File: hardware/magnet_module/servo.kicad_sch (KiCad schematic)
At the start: 5 parts, among them J21 Conn_01x03_Pin, J4 Conn_01x03_Pin, U6 TXB0102DCU

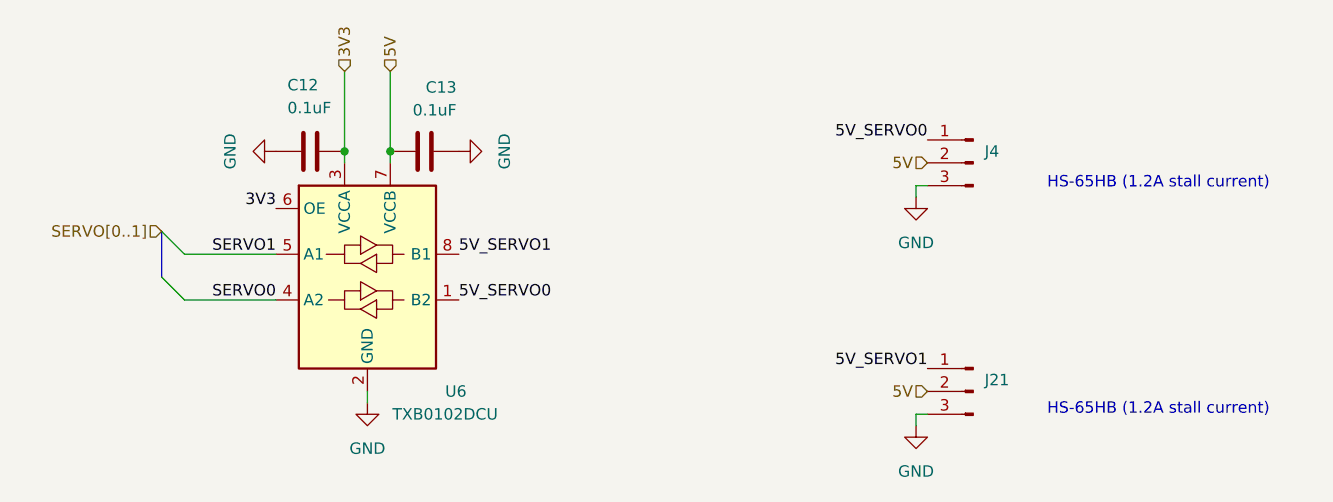
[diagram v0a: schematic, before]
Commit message: Make schematic changes for the following v1.1 changes: * Add directional & latching connector to GPIO0 & GPIO1 * Add CAN IN / CAN OUT directionality * Add pulldown to BOOT pin and pullup to nRST * Correct servo orientation
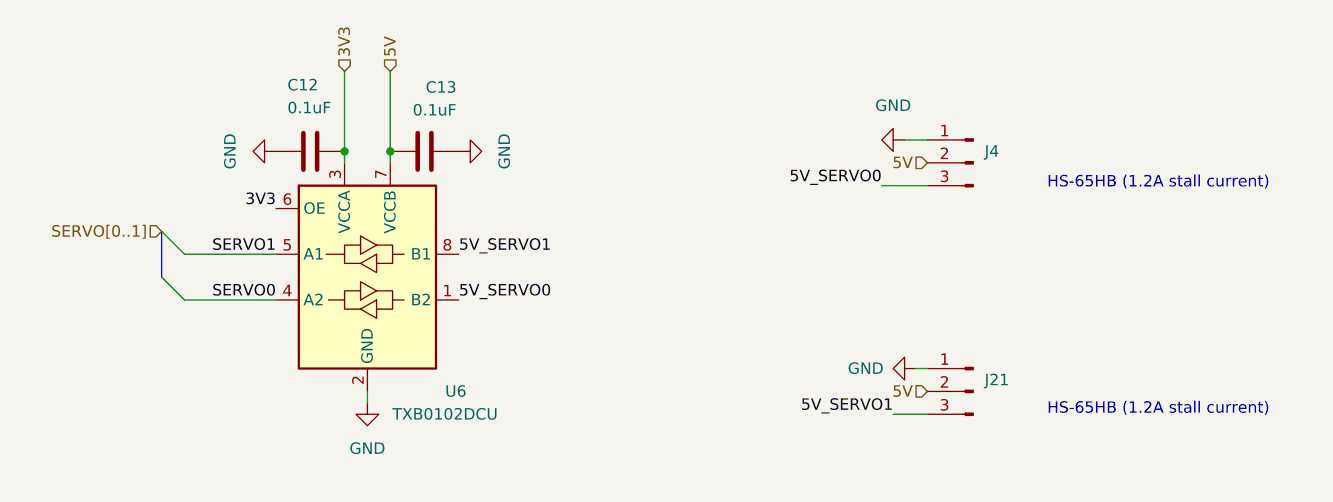
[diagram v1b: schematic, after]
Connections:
- net 5V_SERVO0: now also J4.3 (Pin_3); no longer J4.1 (Pin_1)
- net 5V_SERVO1: now also J21.3 (Pin_3); no longer J21.1 (Pin_1)
- net GND: now also J21.1 (Pin_1), J4.1 (Pin_1); no longer J21.3 (Pin_3), J4.3 (Pin_3)
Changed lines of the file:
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@@
+	(wire
+		(pts
+			(xy 125.73 96.52) (xy 128.27 96.52)
+		)
+		(stroke
+			(width 0)
+			(type default)
+		)
+	)
 	(wire
 		(pts
@@
 	(wire
 		(pts
-			(xy 127 101.6) (xy 127 102.87)
+			(xy 128.27 121.92) (xy 127 121.92)
 		)
 		(stroke
@@
 	(wire
 		(pts
-			(xy 128.27 127) (xy 127 127)
+			(xy 45.72 109.22) (xy 55.88 109.22)
 		)
 		(stroke
@@
 	(wire
 		(pts
-			(xy 45.72 109.22) (xy 55.88 109.22)
+			(xy 124.46 127) (xy 128.27 127)
 		)
 		(stroke
@@
 	(wire
 		(pts
-			(xy 128.27 101.6) (xy 127 101.6)
+			(xy 128.27 101.6) (xy 123.19 101.6)
 		)
 		(stroke
@@
 		)
 	)
-	(wire
-		(pts
-			(xy 127 127) (xy 127 128.27)
-		)
-		(stroke
-			(width 0)
-			(type default)
-		)
-	)
 	(text "HS-65HB (1.2A stall current)"
 		(exclude_from_sim no)
@@
 	)
 	(label "5V_SERVO1"
-		(at 128.27 121.92 180)
+		(at 124.46 127 180)
 		(fields_autoplaced yes)
 		(effects
@@
 	)
 	(label "5V_SERVO0"
-		(at 128.27 96.52 180)
+		(at 123.19 101.6 180)
 		(fields_autoplaced yes)
 		(effects
@@
 	(symbol
 		(lib_id "power:GND")
-		(at 127 102.87 0)
+		(at 125.73 96.52 270)
 		(unit 1)
 		(exclude_from_sim no)
@@
 		(fields_autoplaced yes)
 		(property "Reference" "#PWR011"
-			(at 127 109.22 0)
+			(at 119.38 96.52 0)
 			(effects
 				(font
@@
 		)
 		(property "Value" "GND"
-			(at 127 107.95 0)
+			(at 124.46 92.71 90)
 			(effects
 				(font
@@
 		)
 		(property "Footprint" ""
-			(at 127 102.87 0)
+			(at 125.73 96.52 0)
 			(effects
 				(font
@@
 		)
 		(property "Datasheet" ""
-			(at 127 102.87 0)
+			(at 125.73 96.52 0)
 			(effects
 				(font
@@
 		)
 		(property "Description" "Power symbol creates a global label with name \"GND\" , ground"
-			(at 127 102.87 0)
+			(at 125.73 96.52 0)
 			(effects
 				(font
@@
 	(symbol
 		(lib_id "power:GND")
-		(at 127 128.27 0)
+		(at 127 121.92 270)
 		(unit 1)
 		(exclude_from_sim no)
@@
 		(on_board yes)
 		(dnp no)
-		(fields_autoplaced yes)
 		(property "Reference" "#PWR079"
-			(at 127 134.62 0)
+			(at 120.65 121.92 0)
 			(effects
 				(font
@@
 		)
 		(property "Value" "GND"
-			(at 127 133.35 0)
+			(at 121.412 121.92 90)
 			(effects
 				(font
@@
 		)
 		(property "Footprint" ""
-			(at 127 128.27 0)
+			(at 127 121.92 0)
 			(effects
 				(font
@@
 		)
 		(property "Datasheet" ""
-			(at 127 128.27 0)
+			(at 127 121.92 0)
 			(effects
 				(font
@@
 		)
 		(property "Description" "Power symbol creates a global label with name \"GND\" , ground"
-			(at 127 128.27 0)
-			(effects
-				(font
+			(at 127 121.92 0)
+			(effects
+				(font

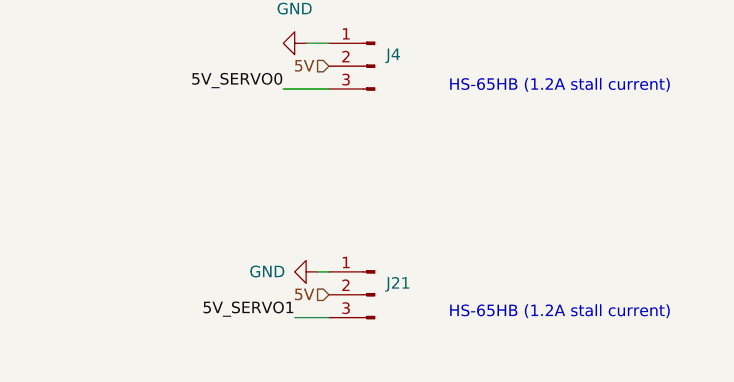
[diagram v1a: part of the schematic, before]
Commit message: Make Alogus-requested mechanical changes
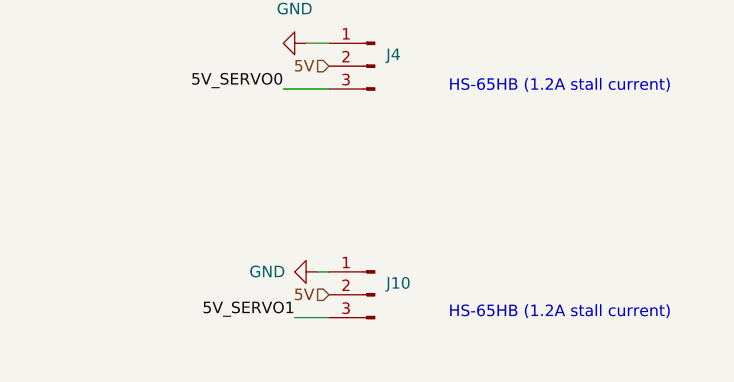
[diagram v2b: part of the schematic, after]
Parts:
- removed J21: Conn_01x03_Pin, Connector_JST:JST_XH_B3B-XH-A_1x03_P2.50mm_Vertical, symbol Connector:Conn_01x03_Pin
- added J10: Conn_01x03_Pin, Connector_JST:JST_XH_S3B-XH-A_1x03_P2.50mm_Horizontal, symbol Connector:Conn_01x03_Pin
- J4: footprint Connector_JST:JST_XH_B3B-XH-A_1x03_P2.50mm_Vertical -> Connector_JST:JST_XH_S3B-XH-A_1x03_P2.50mm_Horizontal; LCSC C144394 -> C157928; MPN B3B-XH-A -> S3B-XH-A
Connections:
- net 5V: now also J10.2 (Pin_2)
- net 5V_SERVO1: now also J10.3 (Pin_3)
- net GND: now also J10.1 (Pin_1)

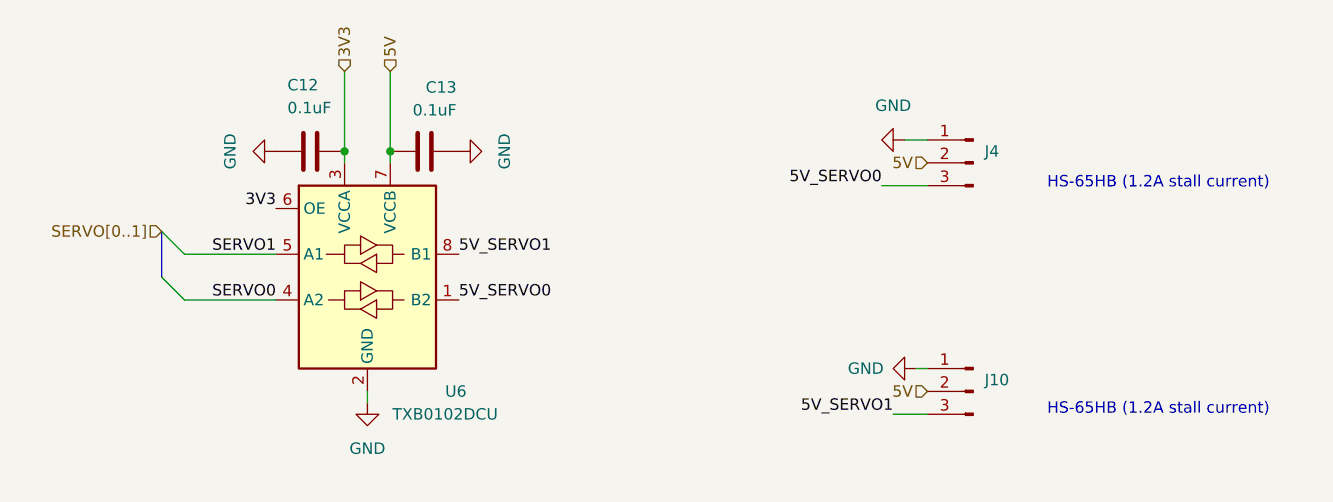
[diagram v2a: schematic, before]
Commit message: add test points to schematic, generate step file including ultrasonic mic
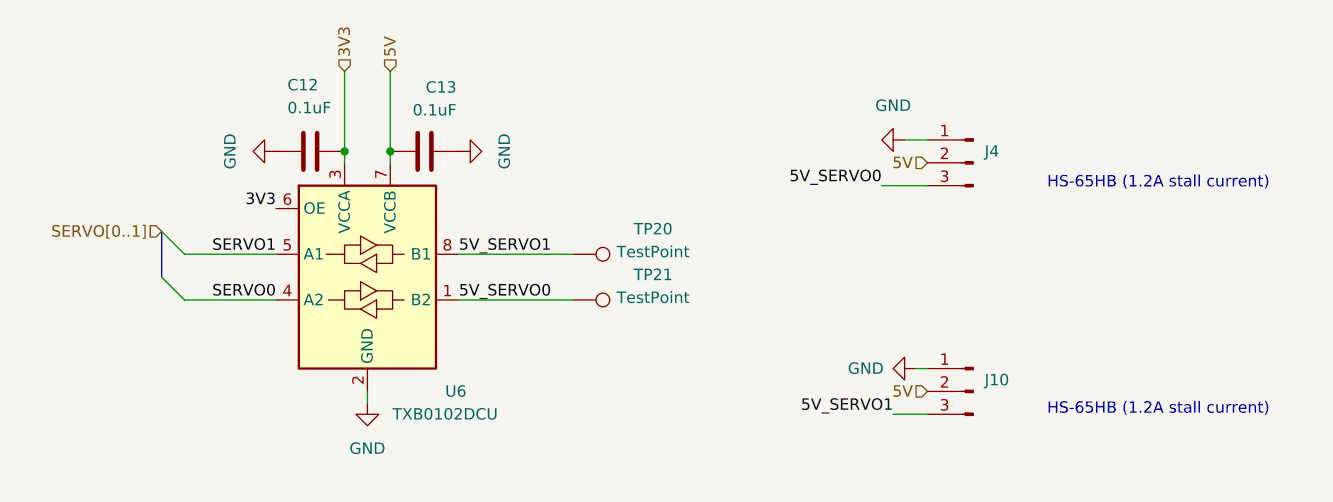
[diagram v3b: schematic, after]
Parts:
- added TP20, TP21: TestPoint, TestPoint:TestPoint_Pad_1.0x1.0mm, symbol Connector:TestPoint
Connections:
- net 5V_SERVO0: now also TP21.1
- net 5V_SERVO1: now also TP20.1
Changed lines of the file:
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@@
+	(wire
+		(pts
+			(xy 88.9 109.22) (xy 76.2 109.22)
+		)
+		(stroke
+			(width 0)
+			(type default)
+		)
+	)
 	(wire
 		(pts
@@
 		(pts
 			(xy 63.5 88.9) (xy 63.5 97.79)
+		)
+		(stroke
+			(width 0)
+			(type default)
+		)
+	)
+	(wire
+		(pts
+			(xy 76.2 114.3) (xy 88.9 114.3)
 		)
 		(stroke
@@
 	)
 	(symbol
+		(lib_id "Connector:TestPoint")
+		(at 88.9 109.22 270)
+		(unit 1)
+		(exclude_from_sim no)
+		(in_bom no)
+		(on_board yes)
+		(dnp no)
+		(property "Reference" "TP20"
+			(at 97.79 106.426 90)
+			(effects
+				(font
+					(size 1.27 1.27)
+				)
+			)
+		)
+		(property "Value" "TestPoint"
+			(at 97.79 108.966 90)
+			(effects
+				(font
+					(size 1.27 1.27)
+				)
+			)
+		)
+		(property "Footprint" "TestPoint:TestPoint_Pad_1.0x1.0mm"
+			(at 88.9 114.3 0)
+			(effects
+				(font
+					(size 1.27 1.27)
+				)
+				(hide yes)
+			)
+		)
+		(property "Datasheet" "~"
+			(at 88.9 114.3 0)
+			(effects
+				(font
+					(size 1.27 1.27)
+				)
+				(hide yes)
+			)
+		)
+		(property "Description" "test point"
+			(at 88.9 109.22 0)
+			(effects
+				(font
+					(size 1.27 1.27)
+				)
+				(hide yes)
+			)
+		)
+		(pin "1"
+		)
+		(instances
+			(project "magnet"
+				(path "/aa5044b8-67cd-4b5a-a593-0df9431eb095/9ed0a7f3-2e3c-4052-98bb-a77cfb577752"
+					(reference "TP20")
+					(unit 1)
+				)
+			)
+		)
+	)
+	(symbol
 		(lib_id "power:GND")
 		(at 125.73 96.52 270)
@@
 					(unit 1)
 				)
+			)
+		)
+	)
+	(symbol
+		(lib_id "Connector:TestPoint")
+		(at 88.9 114.3 270)
+		(unit 1)
+		(exclude_from_sim no)
+		(in_bom no)
+		(on_board yes)
+		(dnp no)
+		(property "Reference" "TP21"
+			(at 97.79 111.506 90)
+			(effects
+				(font
+					(size 1.27 1.27)
+				)
+			)
+		)
+		(property "Value" "TestPoint"
+			(at 97.79 114.046 90)
+			(effects
+				(font
+					(size 1.27 1.27)
+				)
+			)
+		)
+		(property "Footprint" "TestPoint:TestPoint_Pad_1.0x1.0mm"
+			(at 88.9 119.38 0)
+			(effects
+				(font
+					(size 1.27 1.27)
+				)
+				(hide yes)
+			)
+		)
+		(property "Datasheet" "~"
+			(at 88.9 119.38 0)
+			(effects
+				(font
+					(size 1.27 1.27)
+				)
+				(hide yes)
+			)
+		)
+		(property "Description" "test point"
+			(at 88.9 114.3 0)
+			(effects
+				(font
+					(size 1.27 1.27)
+				)
+				(hide yes)
+			)
+		)
+		(pin "1"
+		)
+		(instances
+			(project "magnet"
+				(path "/aa5044b8-67cd-4b5a-a593-0df9431eb095/9ed0a7f3-2e3c-4052-98bb-a77cfb577752"
+					(reference "TP21")
+					(unit 1)
+				)
